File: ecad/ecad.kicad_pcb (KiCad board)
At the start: 4 copper layers, 33.5 x 50 mm, 52 parts, among them J1 USB_C, J3 POWER, J4 Conn_02x10_Top_Bottom, Q1 DMN3009SFG, Q2 DMN3009SFG, SW1 RESET, SW2 BOOT, U1 TPD4E02B04DQA, U2 AP33772S, U3 AP63203WU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

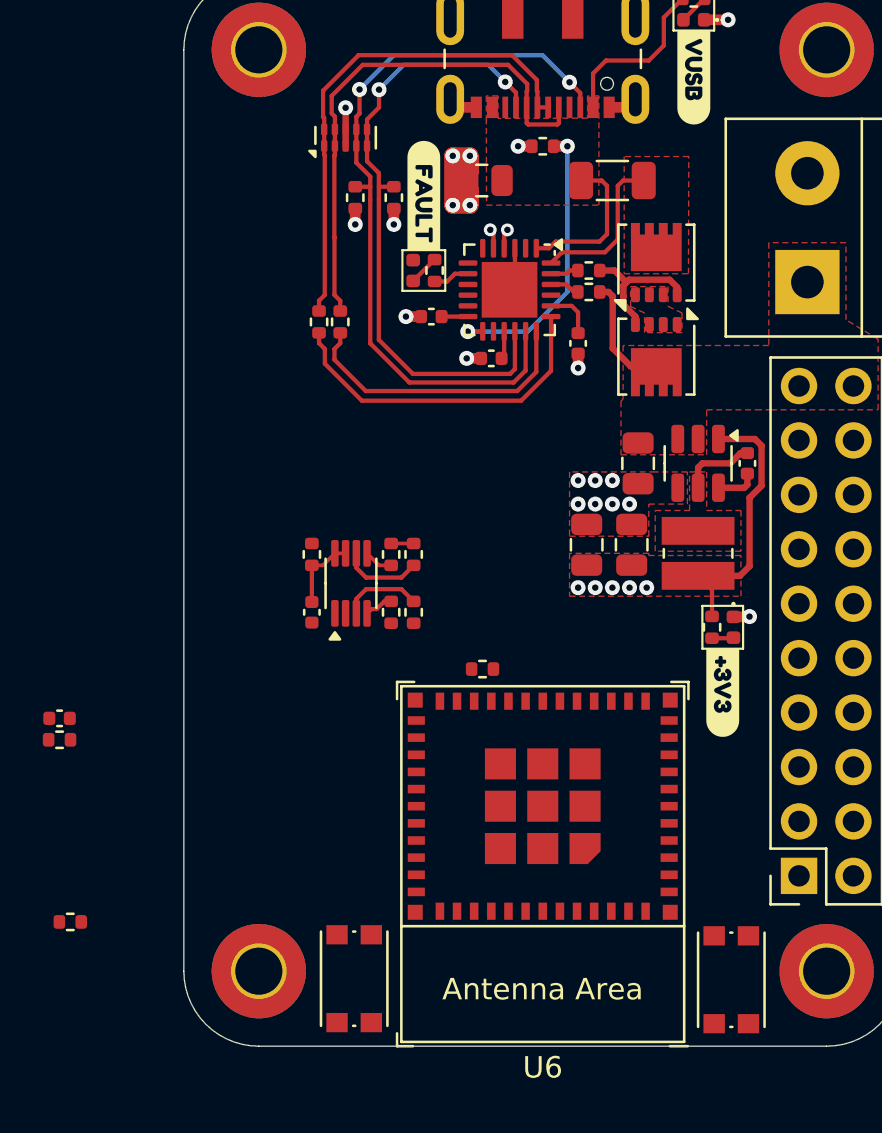
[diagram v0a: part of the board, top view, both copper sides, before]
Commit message: ecad: 4 layers setup and more routing
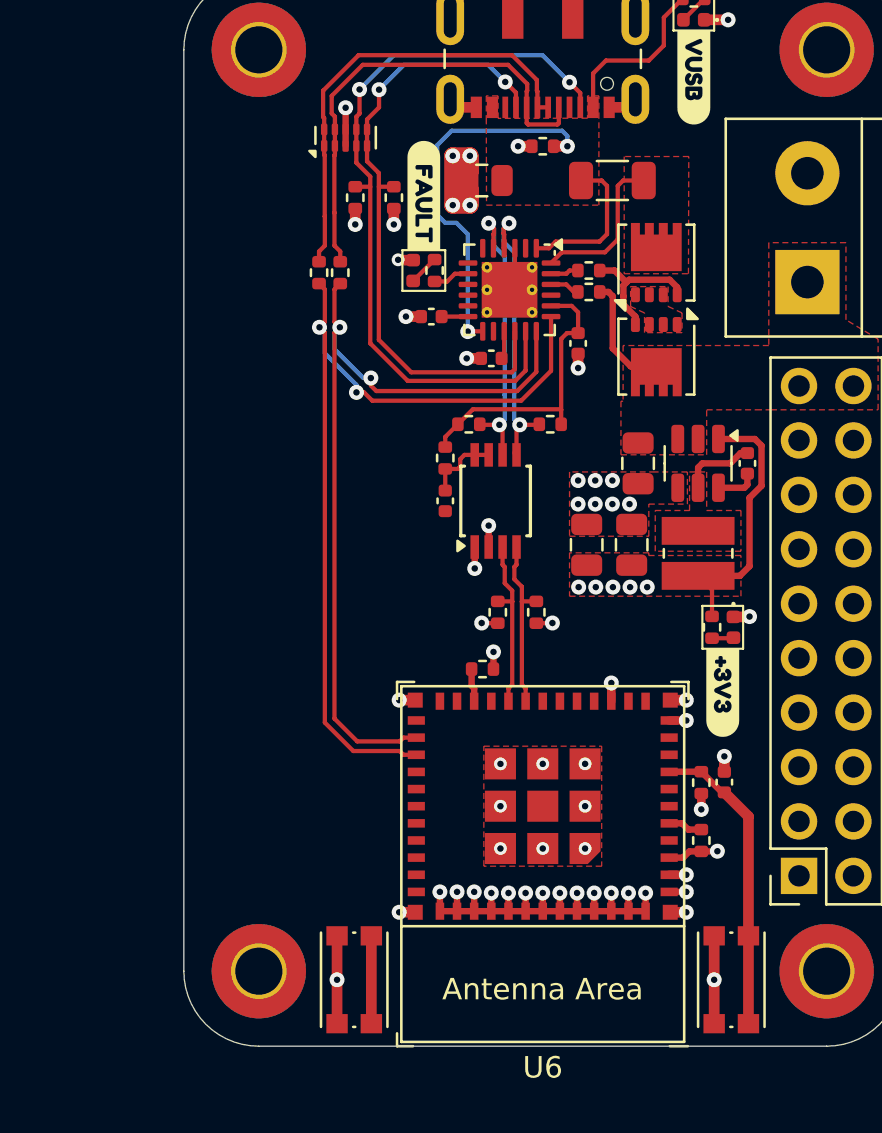
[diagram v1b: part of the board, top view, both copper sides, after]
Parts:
- U2: footprint Package_DFN_QFN:WQFN-24-1EP_4x4mm_P0.5mm_EP2.6x2.6mm -> Package_DFN_QFN:WQFN-24-1EP_4x4mm_P0.5mm_EP2.6x2.6mm_ThermalVias
- U4: footprint Package_SO:VSSOP-8_2.3x2mm_P0.5mm -> Package_SO:TSSOP-8_3x3mm_P0.65mm
- moved C10 31.2 mm to (113.0, 184.3), turned to -90 degrees
- moved R16 30.0 mm to (112.0, 184.4), turned to 90 degrees
- moved R17 29.7 mm to (112.0, 187.1), turned to -90 degrees
- moved R10 9.59 mm to (104.9, 167.6), turned to 180 degrees
- moved C6 8.11 mm to (100.0, 171.2)
- moved U4 7.77 mm to (102.3, 171.2)
- moved R12 7.68 mm to (100.0, 169.2)
- moved R14 6.78 mm to (104.2, 176.4)
- moved R11 6.60 mm to (101.1, 167.6), turned to 0 degrees
- moved R13 3.92 mm to (102.5, 176.4)
- moved R1 2.30 mm to (95.1, 160.6)
- moved R2 2.30 mm to (94.1, 160.6)
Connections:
- net Net-(U4-SCL1) renamed /I2C+
- net Net-(U4-SDA1) renamed /I2C-
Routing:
- net GND: track 23.6 -> 61.0 mm, vias 20 -> 54
- net DP: track 15.9 -> 41.8 mm, vias 0 -> 2
- net DN: track 13.7 -> 38.8 mm, vias 0 -> 2
- net Net-(U6-EN/CHIP_PU): track 0.00 -> 14.2 mm
- net Net-(U2-SDA): track 2.28 -> 14.0 mm, vias 1 -> 2
- net +5V: track 3.41 -> 13.5 mm
- net Net-(U2-SCL): track 4.70 -> 13.8 mm, vias 1 -> 2
- net /I2C-: track 1.36 -> 8.13 mm
- net +3V3: track 12.7 -> 19.2 mm, vias 5 -> 11
- net /I2C+: track 3.77 -> 8.13 mm
- net Net-(U2-OTP): track 13.6 -> 17.9 mm
- net Net-(U6-GPIO9): track 0.00 -> 4.10 mm
- net D-: track 24.4 -> 22.1 mm
- net D+: track 23.4 -> 21.1 mm
- net Net-(U6-GPIO2/ADC1_CH2): track 0.00 -> 1.63 mm
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
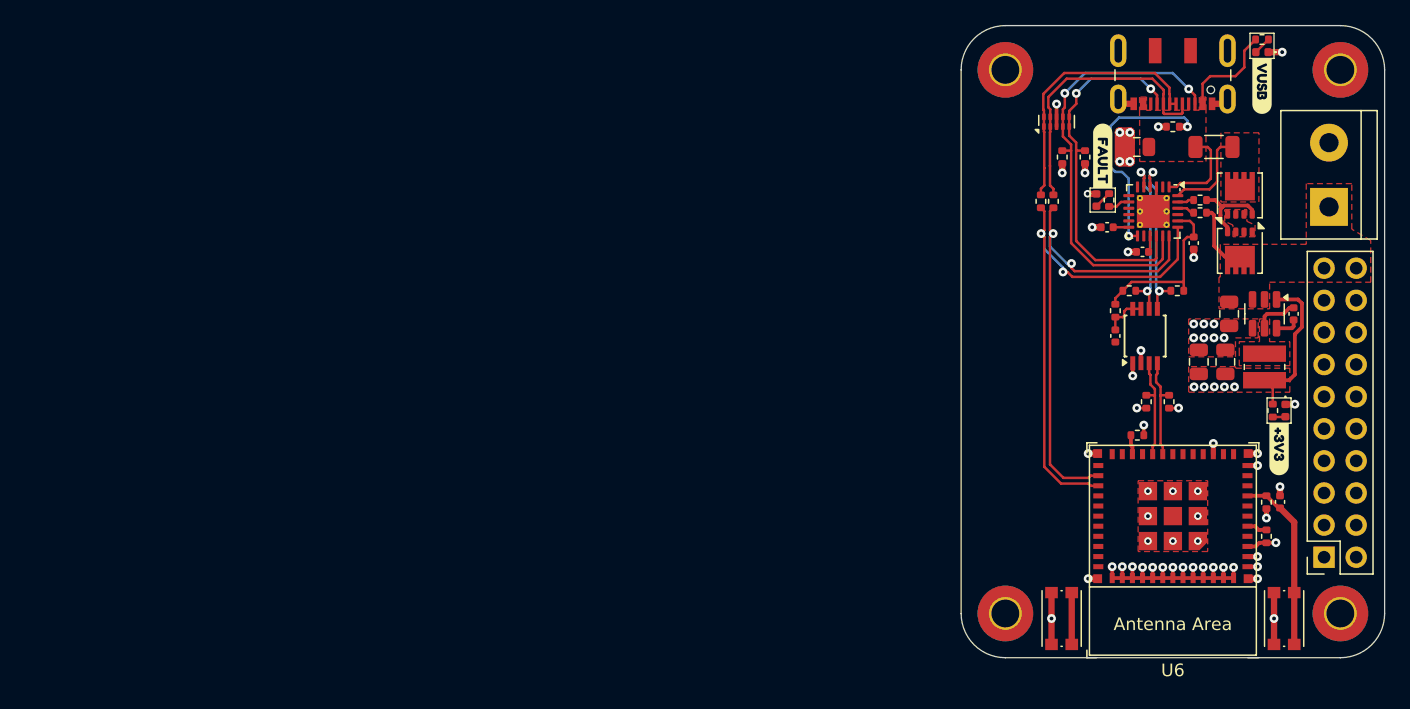
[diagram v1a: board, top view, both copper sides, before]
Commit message: ecad fix: board placement and page template
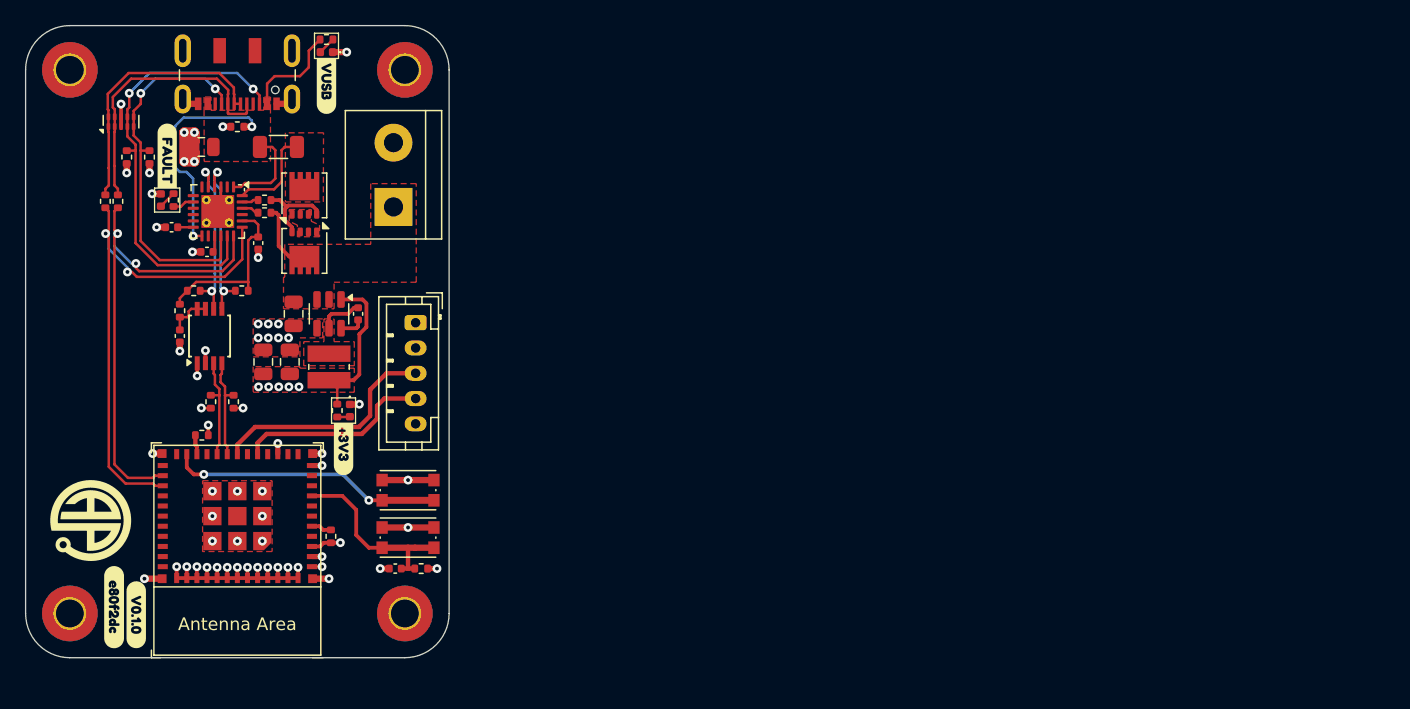
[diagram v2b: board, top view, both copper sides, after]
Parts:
- removed J4: Conn_02x10_Top_Bottom, Connector_PinSocket_2.54mm:PinSocket_2x10_P2.54mm_Vertical
- added J2: Printer, Connector_JST:JST_PH_B5B-PH-K_1x05_P2.00mm_Vertical, F.Cu at (44.6, 170.2)
- added kibuzzard-6820DD34: G***, kibuzzard-6820DD34, F.Cu at (22.6, 193.3)
- added kibuzzard-6820DD4F: G***, kibuzzard-6820DD4F, F.Cu at (20.8, 192.7)
- moved C1 74.0 mm to (27.7, 156.3)
- moved C2 74.0 mm to (25.4, 162.6)
- moved C3 74.0 mm to (28.1, 164.6)
- moved C4 74.0 mm to (35.0, 169.5)
- moved C5 74.0 mm to (32.2, 163.9)
- moved C6 74.0 mm to (26.0, 171.2)
- moved C7 74.0 mm to (32.6, 173.3)
- moved C8 74.0 mm to (40.1, 169.5)
- moved C9 74.0 mm to (34.7, 173.3)
- moved D1 74.0 mm to (37.6, 148.8)
- moved D2 74.0 mm to (24.5, 160.5)
- moved D3 74.0 mm to (39.5, 177.1)
- moved H1 74.0 mm to (43.8, 193.2)
- moved H2 74.0 mm to (17.3, 193.2)
- moved H3 74.0 mm to (43.8, 150.2)
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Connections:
- U6 pad 16: unconnected-(U6-GPIO10-Pad16) -> RX
- U6 pad 6: RX -> unconnected-(U6-GPIO3/ADC1_CH3-Pad6)
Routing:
- net TX: track 0.00 -> 18.4 mm
- net Net-(U6-GPIO9): track 4.10 -> 21.7 mm, vias 0 -> 2
- net RX: track 0.00 -> 15.4 mm
- net GND: track 61.0 -> 62.9 mm, vias 54 -> 55
- net Net-(U6-EN/CHIP_PU): track 14.2 -> 15.2 mm

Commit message: ecad fix: fix bad connection to usb
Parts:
- moved R2 7.21 mm to (23.0, 167.2), turned to 0 degrees
- moved R1 5.77 mm to (23.0, 166.0), turned to 0 degrees
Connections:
- U6 pad 26: DN -> D-
- U6 pad 27: DP -> D+
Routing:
- net DP: track 41.8 -> 10.8 mm, vias 2 -> 0
- net D+: track 21.1 -> 51.3 mm, vias 0 -> 2
- net DN: track 38.8 -> 8.97 mm, vias 2 -> 0
- net D-: track 22.1 -> 49.5 mm, vias 0 -> 1
- net VCC: vias 0 -> 26
- added copper zone on B.Cu, net VCC
- added copper zone on In1.Cu, net VCC
- added copper zone on In2.Cu, net VCC

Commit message: ecad: change ecad version to v0.2
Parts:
- removed kibuzzard-6820DD34: G***, kibuzzard-6820DD34
- removed kibuzzard-6820DD4F: G***, kibuzzard-6820DD4F
- added kibuzzard-68324C86: G***, kibuzzard-68324C86, F.Cu at (22.6, 193.6)
- added kibuzzard-68324D05: G***, kibuzzard-68324D05, F.Cu at (20.8, 192.7)
